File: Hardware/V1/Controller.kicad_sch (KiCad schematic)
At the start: 37 parts, among them Y301 ABM8G-12.000MHZ-4Y-T3

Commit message: motherboard update
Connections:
- net H4: no longer names the net of uC301.15 (GPIO12)
- net H5: no longer names the net of uC301.16 (GPIO13)
- net H6: no longer names the net of uC301.17 (GPIO14)
- net H7: no longer names the net of uC301.18 (GPIO15)
- net cs_lan: no longer names the net of uC301.28 (GPIO17)
- net cs_sd: no longer names the net of uC301.27 (GPIO16)
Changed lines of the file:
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@@
-		)
-	)
-	(label "H4"
-		(at 175.26 146.05 270)
-		(fields_autoplaced yes)
-		(effects
-			(font
-				(size 1.27 1.27)
-			)
-			(justify right bottom)
 		)
 	)
@@
 		)
 	)
-	(label "H5"
-		(at 177.8 146.05 270)
-		(fields_autoplaced yes)
-		(effects
-			(font
-				(size 1.27 1.27)
-			)
-			(justify right bottom)
-		)
-	)
 	(label "RUN"
 		(at 203.2 143.51 270)
@@
 		)
 	)
-	(label "H7"
-		(at 182.88 146.05 270)
-		(fields_autoplaced yes)
-		(effects
-			(font
-				(size 1.27 1.27)
-			)
-			(justify right bottom)
-		)
-	)
 	(label "QSPI_SD1"
 		(at 180.34 64.77 90)
@@
 			)
 			(justify left bottom)
-		)
-	)
-	(label "H6"
-		(at 180.34 146.05 270)
-		(fields_autoplaced yes)
-		(effects
-			(font
-				(size 1.27 1.27)
-			)
-			(justify right bottom)
 		)
 	)
@@
 		)
 	)
-	(hierarchical_label "cs_sd"
-		(shape bidirectional)
-		(at 205.74 146.05 270)
-		(fields_autoplaced yes)
-		(effects
-			(font
-				(size 1.27 1.27)
-			)
-			(justify right)
-		)
-	)
-	(hierarchical_label "cs_lan"
-		(shape bidirectional)
-		(at 208.28 146.05 270)
-		(fields_autoplaced yes)
-		(effects
-			(font
-				(size 1.27 1.27)
-			)
-			(justify right)
-		)
-	)

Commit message: added keys
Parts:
- removed TP301, TP302, TP303: TestPoint, TestPoint:TestPoint_Pad_D1.0mm, symbol SymbolsBalloonv4:TestPoint
- removed uC301: SC0914_7_, QFN40P700X700X90-57N-D, symbol SymbolsBalloonv4:SC0914_7_
- added J5: MEM2085-00-115-00-A, SamacSys_Parts:MEM20850011500A, symbol SamacSys_Parts:MEM2085-00-115-00-A
- added JuC1: SC0914_7_, SamacSys_Parts:QFN40P700X700X90-57N-D, symbol SamacSys_Parts:SC0914_7_
- S_BOOT301: footprint 435441019830 -> SamacSys_Parts:435441019830
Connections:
- net +1V1: now also JuC1.23 (DVDD_1), JuC1.45 (VREG_VOUT), JuC1.50 (DVDD_2)
- net 3V3: now also JuC1.1 (IOVDD_1), JuC1.10 (IOVDD_2), JuC1.22 (IOVDD_3), JuC1.26 (RUN), JuC1.33 (IOVDD_4), JuC1.42 (IOVDD_5), JuC1.44 (VREG_VIN), JuC1.48 (USB_VDD), JuC1.49 (IOVDD_6)
- net A1: now also JuC1.39 (GPIO27/ADC1)
- net A2: now also JuC1.40 (GPIO28/ADC2)
- net A3: now also JuC1.41 (GPIO29/ADC3)
- net GND: now also JuC1.19 (TESTEN), JuC1.57 (GND)
- net GPIO0: now also JuC1.2 (GPIO0)
- net GPIO1: now also JuC1.3 (GPIO1)
- net QSPI_SCLK: now also JuC1.52 (QSPI_SCLK)
- net QSPI_SD0: now also JuC1.53 (QSPI_SD0)
- net QSPI_SD1: now also JuC1.55 (QSPI_SD1)
- net QSPI_SD2: now also JuC1.54 (QSPI_SD2)
- net QSPI_SD3: now also JuC1.51 (QSPI_SD3)
- net QSPI_SS: now also JuC1.56 (QSPI_SS_N)
- net XIN: now also JuC1.20 (XIN)
- net XOUT: now also JuC1.21 (XOUT)
- net at R0.2: now also JuC1.35 (GPIO23)
- net at C308.1, R305.2: now also JuC1.43 (ADC_AVDD)
- net at R302.2: now also JuC1.47 (USB_DP)
- net at R303.2: now also JuC1.46 (USB_DM)
- no-connect marks 2 -> 4
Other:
- moved on the sheet: C1, C2, LRuC1

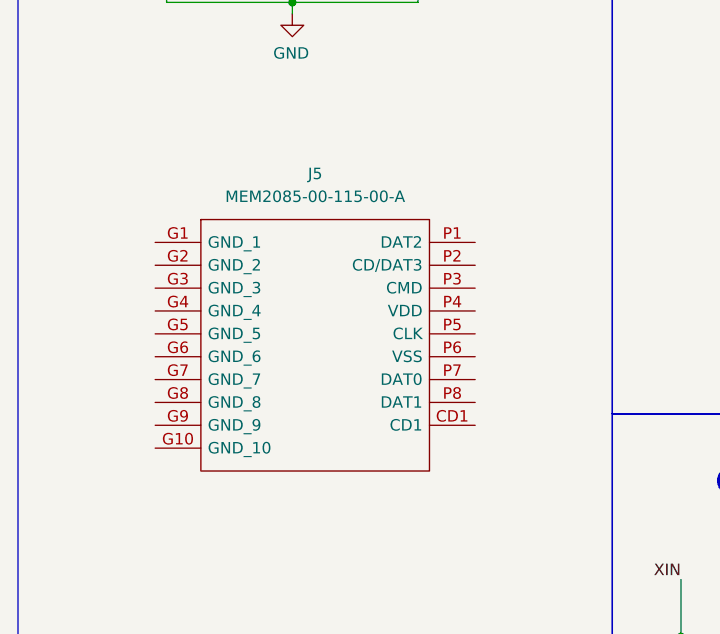
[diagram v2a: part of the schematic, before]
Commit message: refined footprint
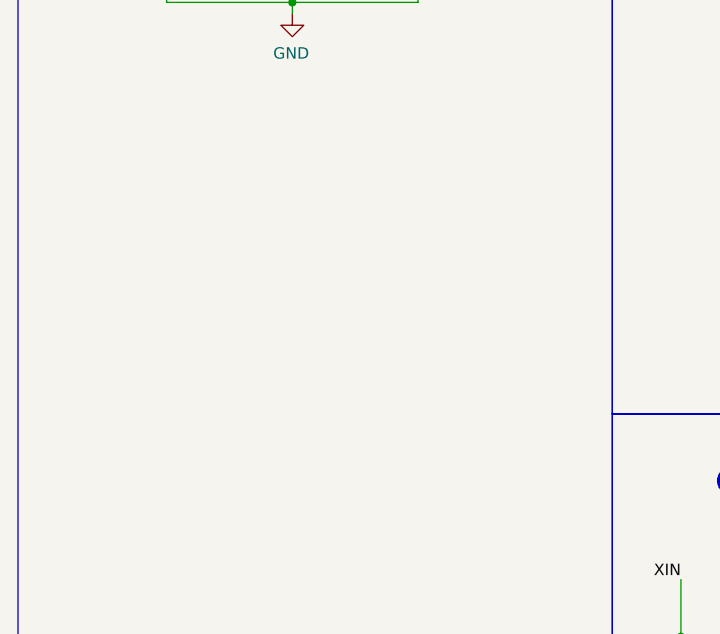
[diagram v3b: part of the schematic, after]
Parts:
- removed J5: MEM2085-00-115-00-A, SamacSys_Parts:MEM20850011500A, symbol SamacSys_Parts:MEM2085-00-115-00-A
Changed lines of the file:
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@@
-	)
-	(symbol
-		(lib_id "SamacSys_Parts:MEM2085-00-115-00-A")
-		(at 29.21 119.38 0)
-		(unit 1)
-		(exclude_from_sim no)
-		(in_bom yes)
-		(on_board yes)
-		(dnp no)
-		(fields_autoplaced yes)
-		(property "Reference" "J5"
-			(at 46.99 111.76 0)
-			(effects
-				(font
-					(size 1.27 1.27)
-				)
-			)
-		)
-		(property "Value" "MEM2085-00-115-00-A"
-			(at 46.99 114.3 0)
-			(effects
-				(font
-					(size 1.27 1.27)
-				)
-			)
-		)
-		(property "Footprint" "SamacSys_Parts:MEM20850011500A"
-			(at 60.96 116.84 0)
-			(effects
-				(font
-					(size 1.27 1.27)
-				)
-				(justify left)
-				(hide yes)
-			)
-		)
-		(property "Datasheet" "https://gct.co/files/drawings/mem2085.pdf"
-			(at 60.96 119.38 0)
-			(effects
-				(font
-					(size 1.27 1.27)
-				)
-				(justify left)
-				(hide yes)
-			)
-		)
-		(property "Description" "Memory Card Connectors Micro SD Push Pull SMT 1.15mm No Peg"
-			(at 29.21 119.38 0)
-			(effects
-				(font
-					(size 1.27 1.27)
-				)
-				(hide yes)
-			)
-		)
-		(property "Description_1" "Memory Card Connectors Micro SD Push Pull SMT 1.15mm No Peg"
-			(at 60.96 121.92 0)
-			(effects
-				(font
-					(size 1.27 1.27)
-				)
-				(justify left)
-				(hide yes)
-			)
-		)
-		(property "Height" "1.35"
-			(at 60.96 124.46 0)
-			(effects
-				(font
-					(size 1.27 1.27)
-				)
-				(justify left)
-				(hide yes)
-			)
-		)
-		(property "Mouser Part Number" "640-MEM20850011500A"
-			(at 60.96 127 0)
-			(effects
-				(font
-					(size 1.27 1.27)
-				)
-				(justify left)
-				(hide yes)
-			)
-		)
-		(property "Mouser Price/Stock" "https://www.mouser.co.uk/ProductDetail/GCT/MEM2085-00-115-00-A?qs=rQFj71Wb1eWNkFUhuuvVIA%3D%3D"
-			(at 60.96 129.54 0)
-			(effects
-				(font
-					(size 1.27 1.27)
-				)
-				(justify left)
-				(hide yes)
-			)
-		)
-		(property "Manufacturer_Name" "GCT (GLOBAL CONNECTOR TECHNOLOGY)"
-			(at 60.96 132.08 0)
-			(effects
-				(font
-					(size 1.27 1.27)
-				)
-				(justify left)
-				(hide yes)
-			)
-		)
-		(property "Manufacturer_Part_Number" "MEM2085-00-115-00-A"
-			(at 60.96 134.62 0)
-			(effects
-				(font
-					(size 1.27 1.27)
-				)
-				(justify left)
-				(hide yes)
-			)
-		)
-		(pin "G2"
-		)
-		(pin "G3"
-		)
-		(pin "CD1"
-		)
-		(pin "G1"
-		)
-		(pin "G10"
-		)
-		(pin "P8"
-		)
-		(pin "P4"
-		)
-		(pin "P5"
-		)
-		(pin "P7"
-		)
-		(pin "P2"
-		)
-		(pin "G7"
-		)
-		(pin "G4"
-		)
-		(pin "G9"
-		)
-		(pin "P6"
-		)
-		(pin "P3"
-		)
-		(pin "G8"
-		)
-		(pin "G5"
-		)
-		(pin "P1"
-		)
-		(pin "G6"
-		)
-		(instances
-			(project "Credit_card_Midi_piano"
-				(path "/fd98d8e1-15f7-4e74-a843-9bd80f80983b/33b036a2-37a7-49ba-bfe3-b178e6a2120d"
-					(reference "J5")
-					(unit 1)
-				)
-			)
-		)
 	)
 	(symbol
